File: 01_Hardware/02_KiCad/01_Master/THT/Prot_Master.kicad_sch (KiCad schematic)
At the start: 16 parts, among them J10 Conn_01x22_Female, J20 Conn_01x22_Female, J5 Screw_Terminal_01x04, J6 Screw_Terminal_01x04, U1 LM393P

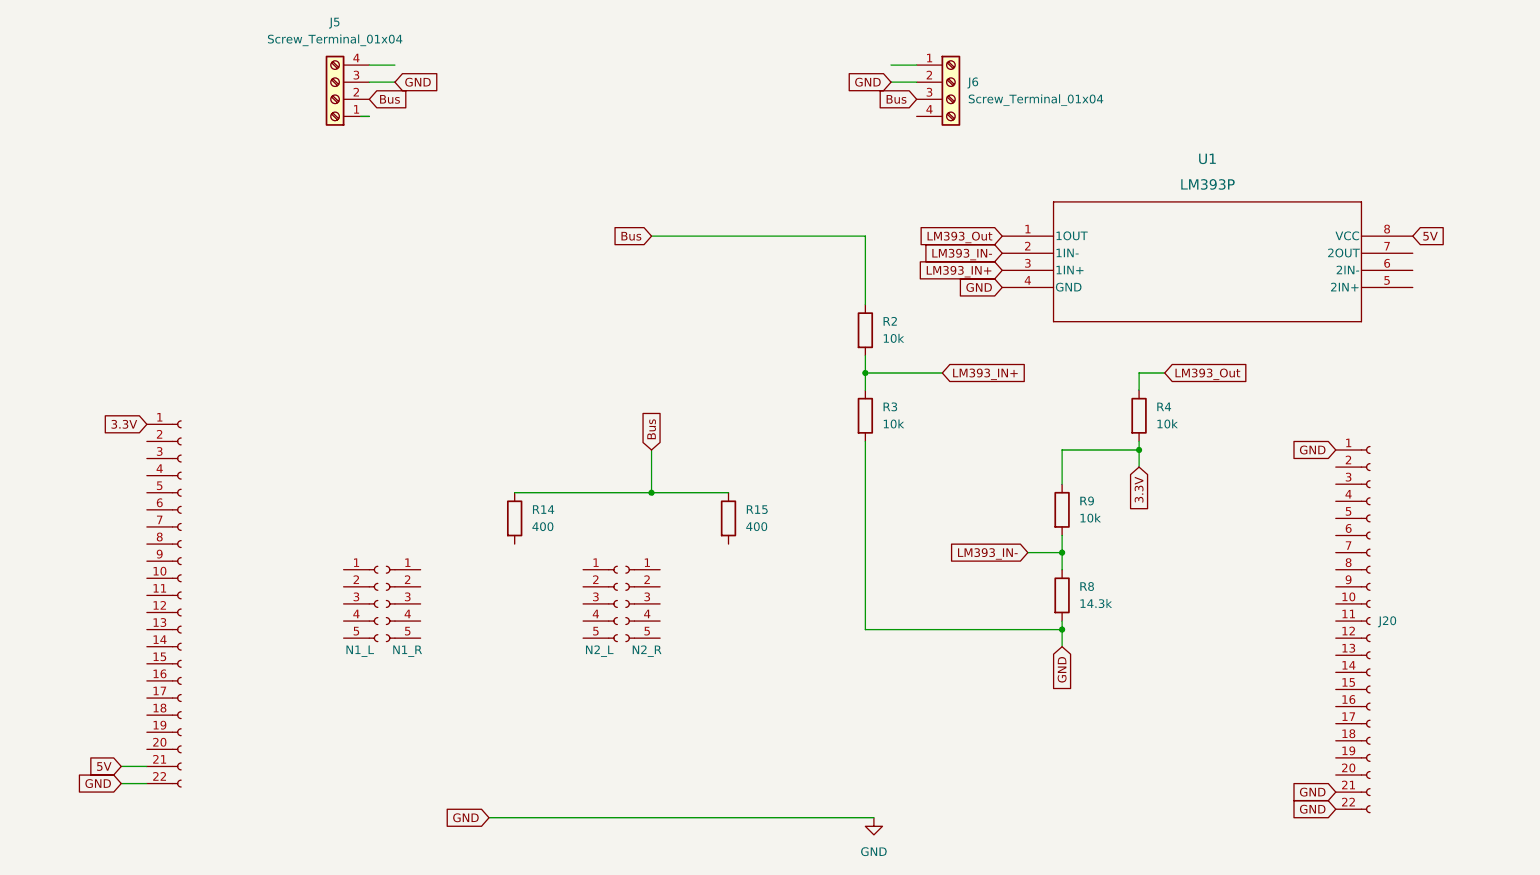
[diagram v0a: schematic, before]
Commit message: Master and Slave Prototyp finsished! JLCPCB ordered
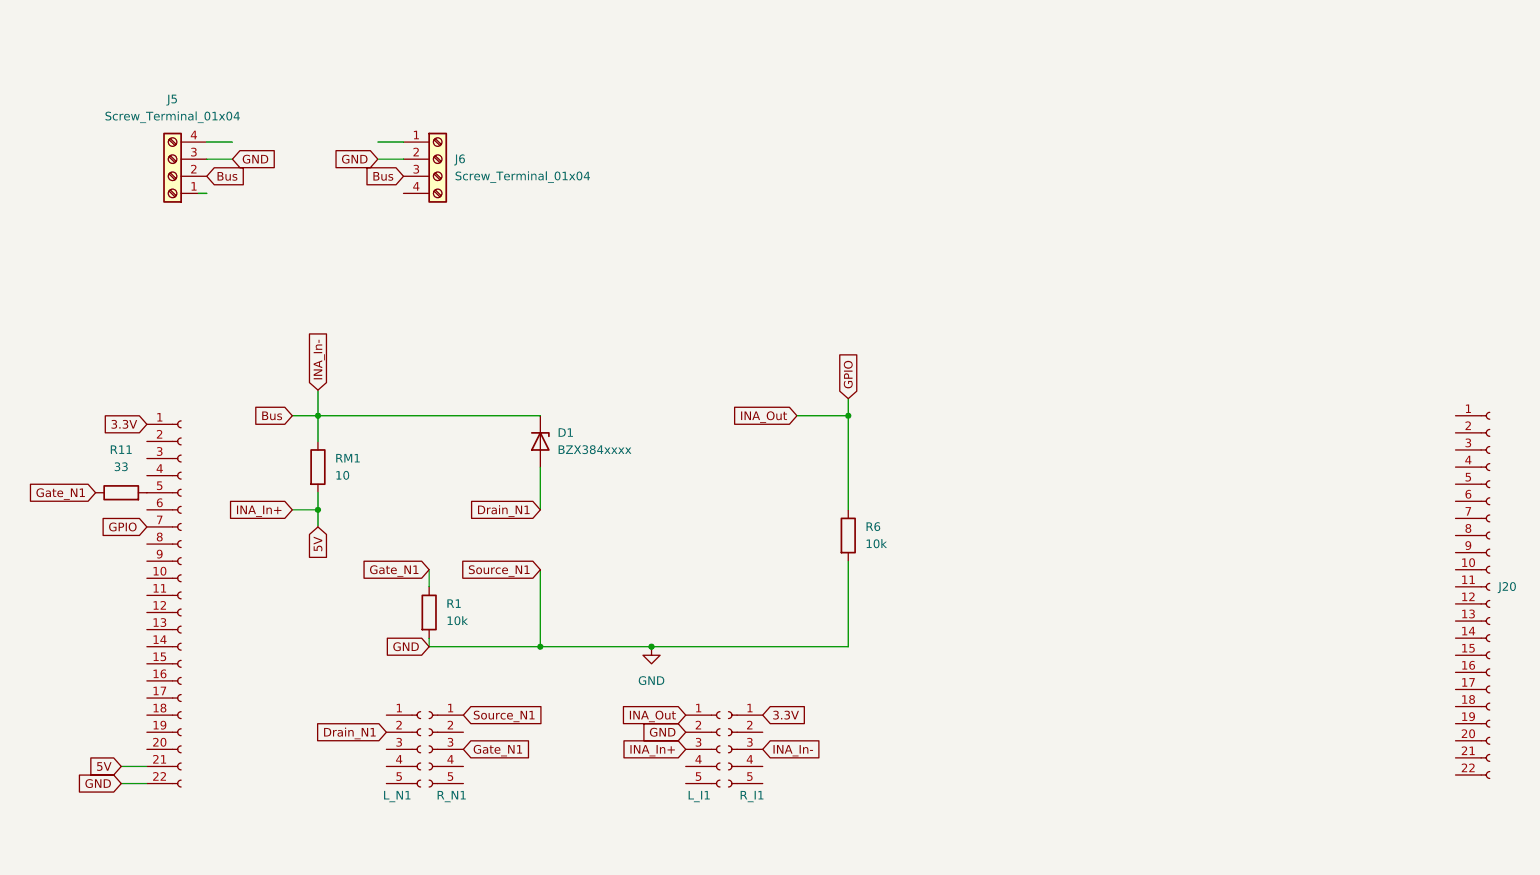
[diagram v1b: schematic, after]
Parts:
- removed N1_R: NMOS2, symbol Connector:Conn_01x05_Socket
- removed R14, R15: 400, Resistor_THT:R_Axial_DIN0204_L3.6mm_D1.6mm_P5.08mm_Horizontal, symbol Device:R
- removed R2, R3, R4, R9: 10k, Resistor_THT:R_Axial_DIN0204_L3.6mm_D1.6mm_P5.08mm_Horizontal, symbol Device:R
- removed R8: 14.3k, Resistor_THT:R_Axial_DIN0204_L3.6mm_D1.6mm_P5.08mm_Horizontal, symbol Device:R
- removed U1: LM393P, LM393:P8, symbol LM393:LM393P
- added D1: BZX384xxxx, Diode_THT:D_A-405_P7.62mm_Horizontal, symbol Diode:BZX384xxxx
- added R1, R6: 10k, Resistor_THT:R_Axial_DIN0204_L3.6mm_D1.6mm_P5.08mm_Horizontal, symbol Device:R
- added R11: 33, Resistor_THT:R_Axial_DIN0204_L3.6mm_D1.6mm_P5.08mm_Horizontal, symbol Device:R
- added RM1: 10, Resistor_THT:R_Axial_DIN0204_L3.6mm_D1.6mm_P5.08mm_Horizontal, symbol Device:R
- added R_N1: NMOS1, Connector_PinSocket_2.54mm:PinSocket_1x05_P2.54mm_Vertical, symbol Connector:Conn_01x05_Socket
- L_I1: renamed from N2_L; footprint (none) -> Connector_PinSocket_2.54mm:PinSocket_1x05_P2.54mm_Vertical
- L_N1: renamed from N1_L; footprint (none) -> Connector_PinSocket_2.54mm:PinSocket_1x05_P2.54mm_Vertical
- R_I1: renamed from N2_R; footprint (none) -> Connector_PinSocket_2.54mm:PinSocket_1x05_P2.54mm_Vertical
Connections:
- net 3.3V: now also R_I1.1 (Pin_1)
- net 5V: now also L_I1.3 (Pin_3), RM1.2
- net Bus: now also R_I1.3 (Pin_3), D1.1 (K), RM1.1
- net GND: now also L_I1.2 (Pin_2), R1.2, R6.2, R_N1.1 (Pin_1); no longer J20.1 (Pin_1), J20.21 (Pin_21), J20.22 (Pin_22)
- net GPIO: now reaches L_I1.1 (Pin_1)
- net GPIO: now also J10.7 (Pin_7), R6.1
- net Drain_N1: now reaches L_N1.2 (Pin_2)
- net Drain_N1: now also D1.2 (A)
- net at J10.5 (Pin_5): now also R11.2
- new net Gate_N1: R1.1, R11.1, R_N1.3 (Pin_3)
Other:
- moved on the sheet: J20, J5, J6, L_I1, L_N1, R_I1
